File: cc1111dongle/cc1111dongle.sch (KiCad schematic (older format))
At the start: 50 parts, among them J1 GSG-900MHZ-F-ANTENNA, J2 GSG-USB-MICRO-B, P1 EXPANSION, P2 ANTENNA, P3 RESET_N, P4 DD, P5 DC, P6 3V3, P7 GND, P8 GOODFET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

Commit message: finished cc1111dongle schematic
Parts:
- removed J1: GSG-900MHZ-F-ANTENNA, symbol GSG-900MHZ-F-ANTENNA
- removed J2: GSG-USB-MICRO-B, symbol GSG-USB-MICRO-B
- removed P1: EXPANSION, symbol CONN_8X2
- removed P2: ANTENNA, symbol GSG-SMA-CONN
- removed P8: GOODFET, symbol CONN_7X2
- removed P9: PWR, symbol CONN_3X2
- removed R15, R7: 0, symbol R-SHORTED
- removed SW1: SW_PUSH, symbol SW_PUSH
- added C18, C25: 22nF, symbol C
- added C19, C20, C21, C22, C23: 100pF, symbol C
- added C24: 1uF, symbol C
- added FB1: FILTER, symbol FILTER
- added J1: USB-DEVICE, symbol USB-DEVICE
- added L1: 1uH, symbol INDUCTOR
- added P1: EXPANSION, symbol CONN_5X2
- added P2: BNC-CONN, symbol BNC-CONN
- added R1, R15: 4k7, symbol R
- added R3: 1k, symbol R
- added R7: 15, symbol R
- added U3, U8: DMC2400, symbol DMC2400
- added U4: RX_AMP, symbol BGA2717
- added U5, U6: SKY13385, symbol SKY13385
- added U7: TX_AMP, symbol BGA616
- C17: value 10nF -> 1uF; Description CAP CER 10000PF 50V 10% X7R 0603 -> CAP CER 1UF 10V 10% X7R 0603; Manufacturer Murata -> Taiyo Yuden; Note DNP -> (none); Part Number GRM188R71H103KA01D -> LMK107B7105KA-T
- C6: value 10nF -> 220pF; Description CAP CER 10000PF 50V 10% X7R 0603 -> CAP CER 220PF 50V 10% X7R 0402; Part Number GRM188R71H103KA01D -> GRM155R71H221KA01D
- C7: value 10nF -> 220pF; Description CAP CER 10000PF 25V 10% X7R 0402 -> CAP CER 220PF 50V 10% X7R 0402; Part Number GRM155R71E103KA01D -> GRM155R71H221KA01D
- D1, D3, D4, R11, R12: Note DNP -> (none)
- R10, R4, R8, R9: Note (none) -> 1%
- R14: value 10k -> 1k; Description RES 10K OHM 1/10W 5% 0603 SMD -> RES 1K OHM 1/16W 5% 0402 SMD; Part Number RMCF0603JT10K0 -> RMCF0402JT1K00
- R2: value 10k -> 4k7; Description RES 10K OHM 1/10W 5% 0603 SMD -> RES 4.7K OHM 1/16W 5% 0402 SMD; Part Number RMCF0603JT10K0 -> RMCF0402JT4K70
- R6: value 0 -> 4k7; Description (none) -> RES 4.7K OHM 1/16W 5% 0402 SMD; Manufacturer (none) -> Stackpole; Note DNP -> (none); Part Number (none) -> RMCF0402JT4K70
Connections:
- net labels added: AMP_BYPASS_EN, RX_AMP_EN, TX_AMP_EN
- net labels removed: P0_4, P0_5, P1_6, P1_7, P2_0
- wire segments 158 -> 200
- no-connect marks 10 -> 2
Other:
- note added: "RX amp path"
- note added: "RX/TX amp bypass path"
- note added: "TX amp path"
- note removed: "programming header matching GoodFET pinout"
- moved on the sheet: C1, C10, C11, C12, C13, C14, C15, C16, C2, C3, C4, C5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

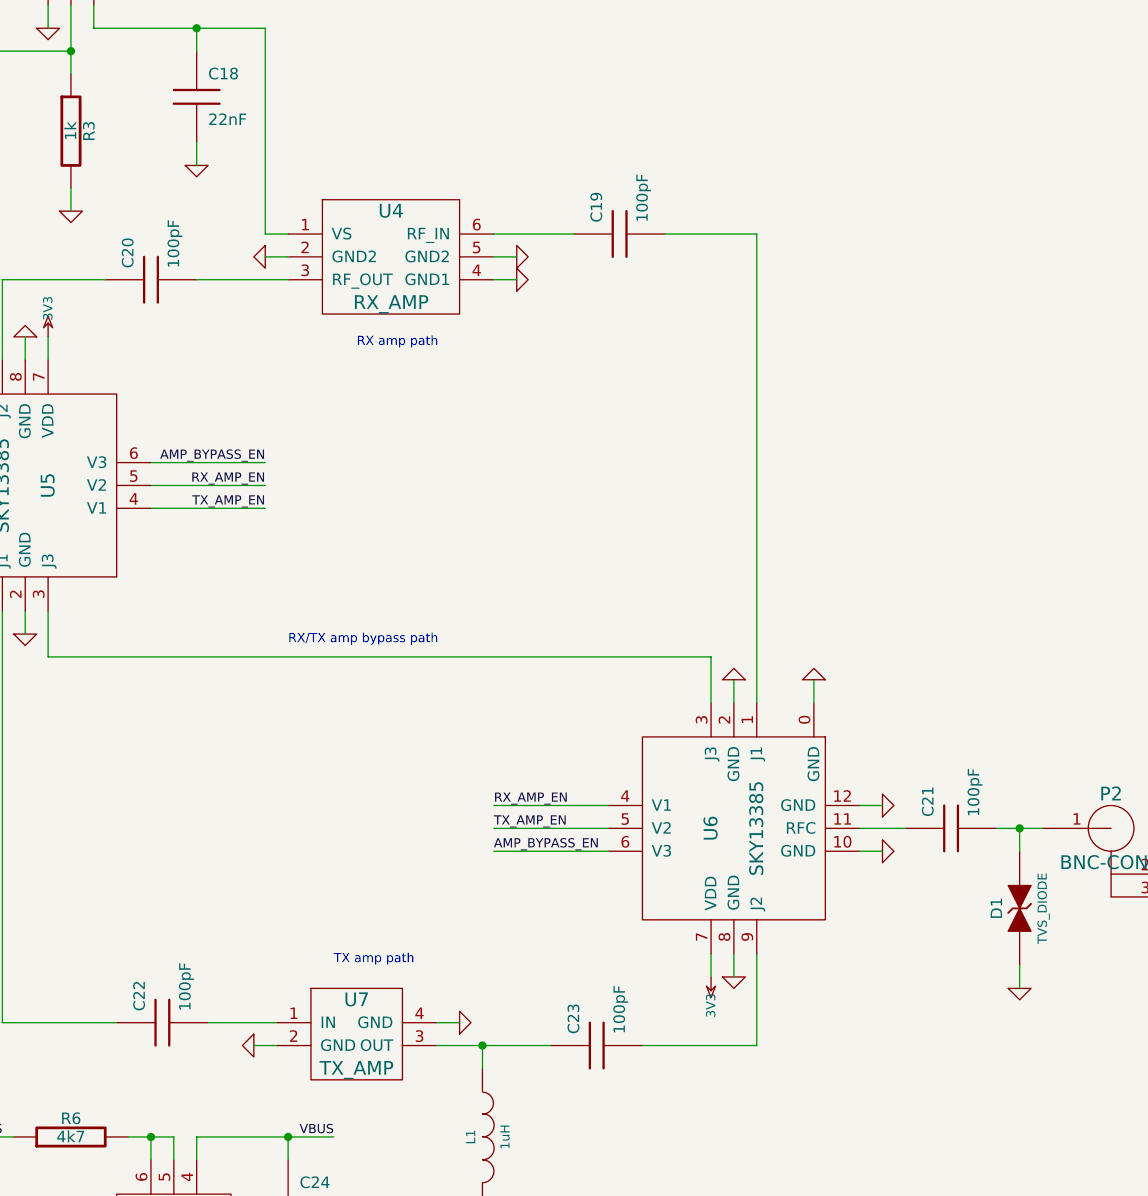
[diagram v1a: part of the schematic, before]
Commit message: replaced some obsolete part numbers
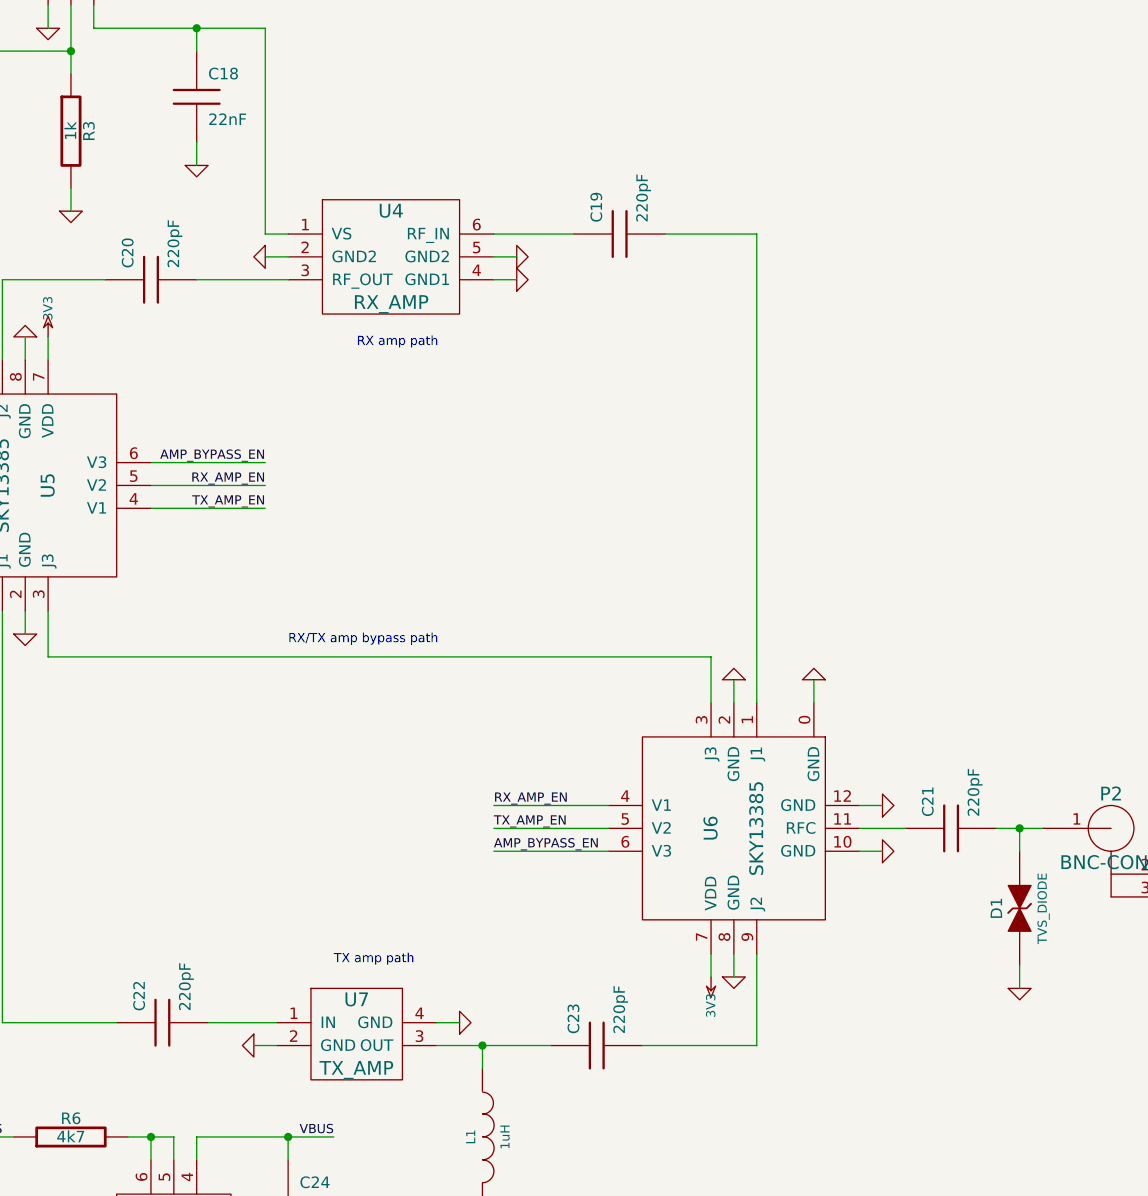
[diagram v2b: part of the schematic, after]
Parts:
- C19, C20, C21, C22, C23: value 100pF -> 220pF; Description CAP CER 100PF 50V 5% NP0 0402 -> CAP CER 220PF 50V 10% X7R 0402; Part Number GRM1555C1H101JZ01D -> GRM155R71H221KA01D
- C9: Manufacturer Murata -> Taiyo Yuden; Part Number GRM1555C1H2R2CZ01D -> UMK105CG2R2CW-F
- U7: Part Number BGA616E6327 -> BGA 616 H6327

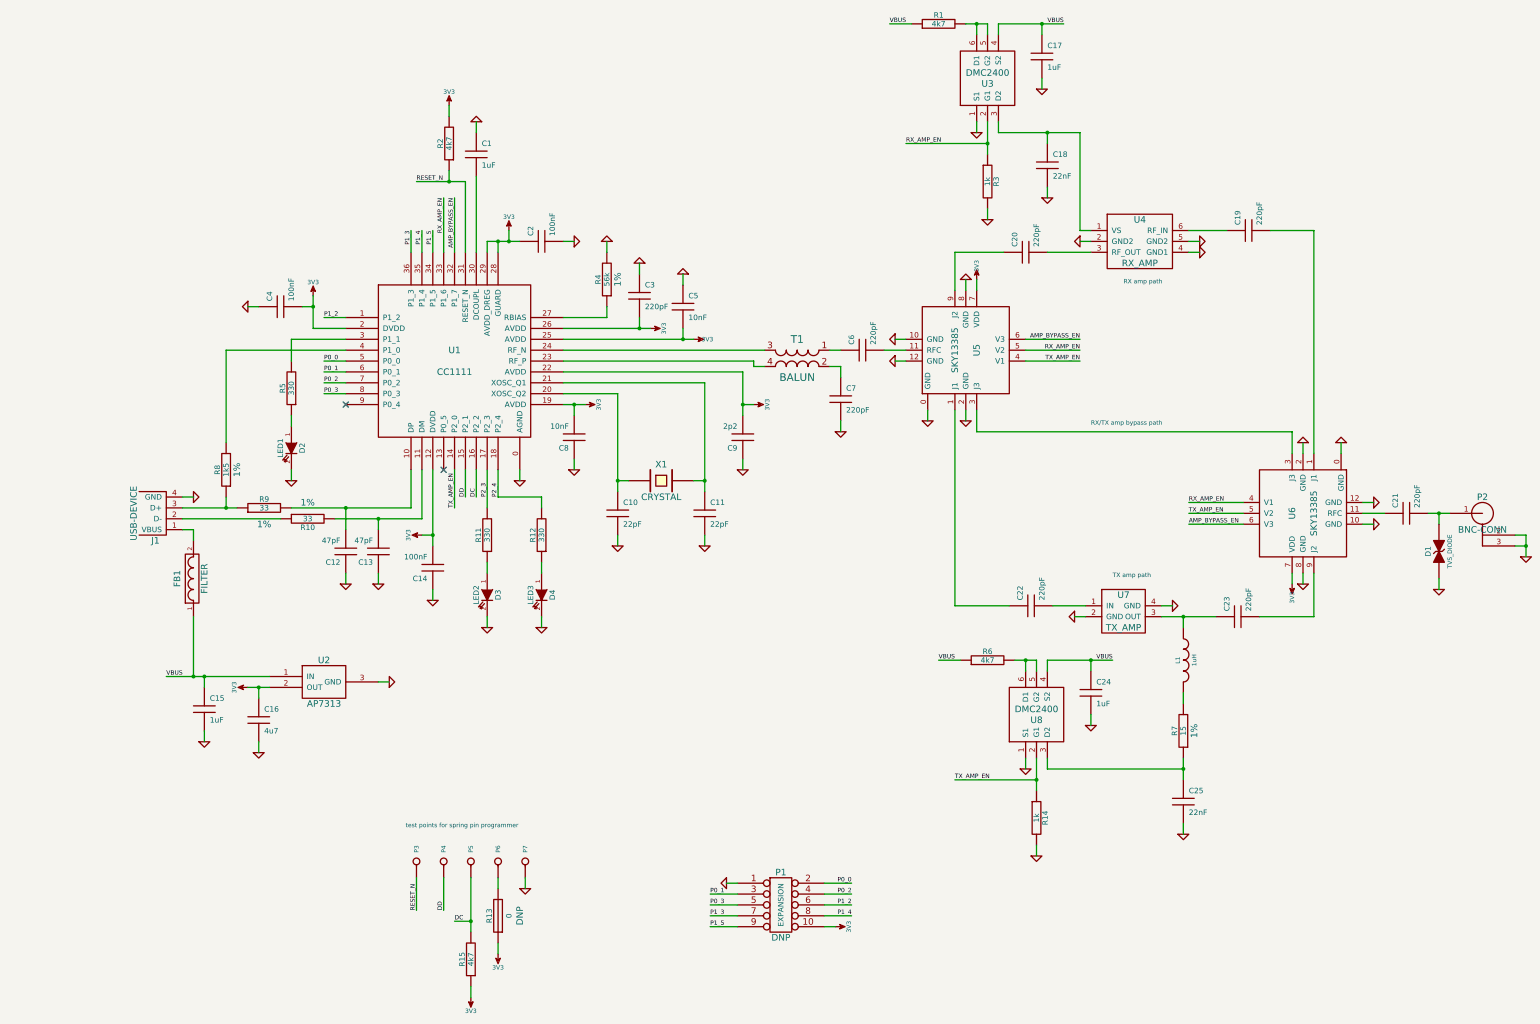
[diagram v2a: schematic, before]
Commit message: extra decoupling based on BGA616 app note
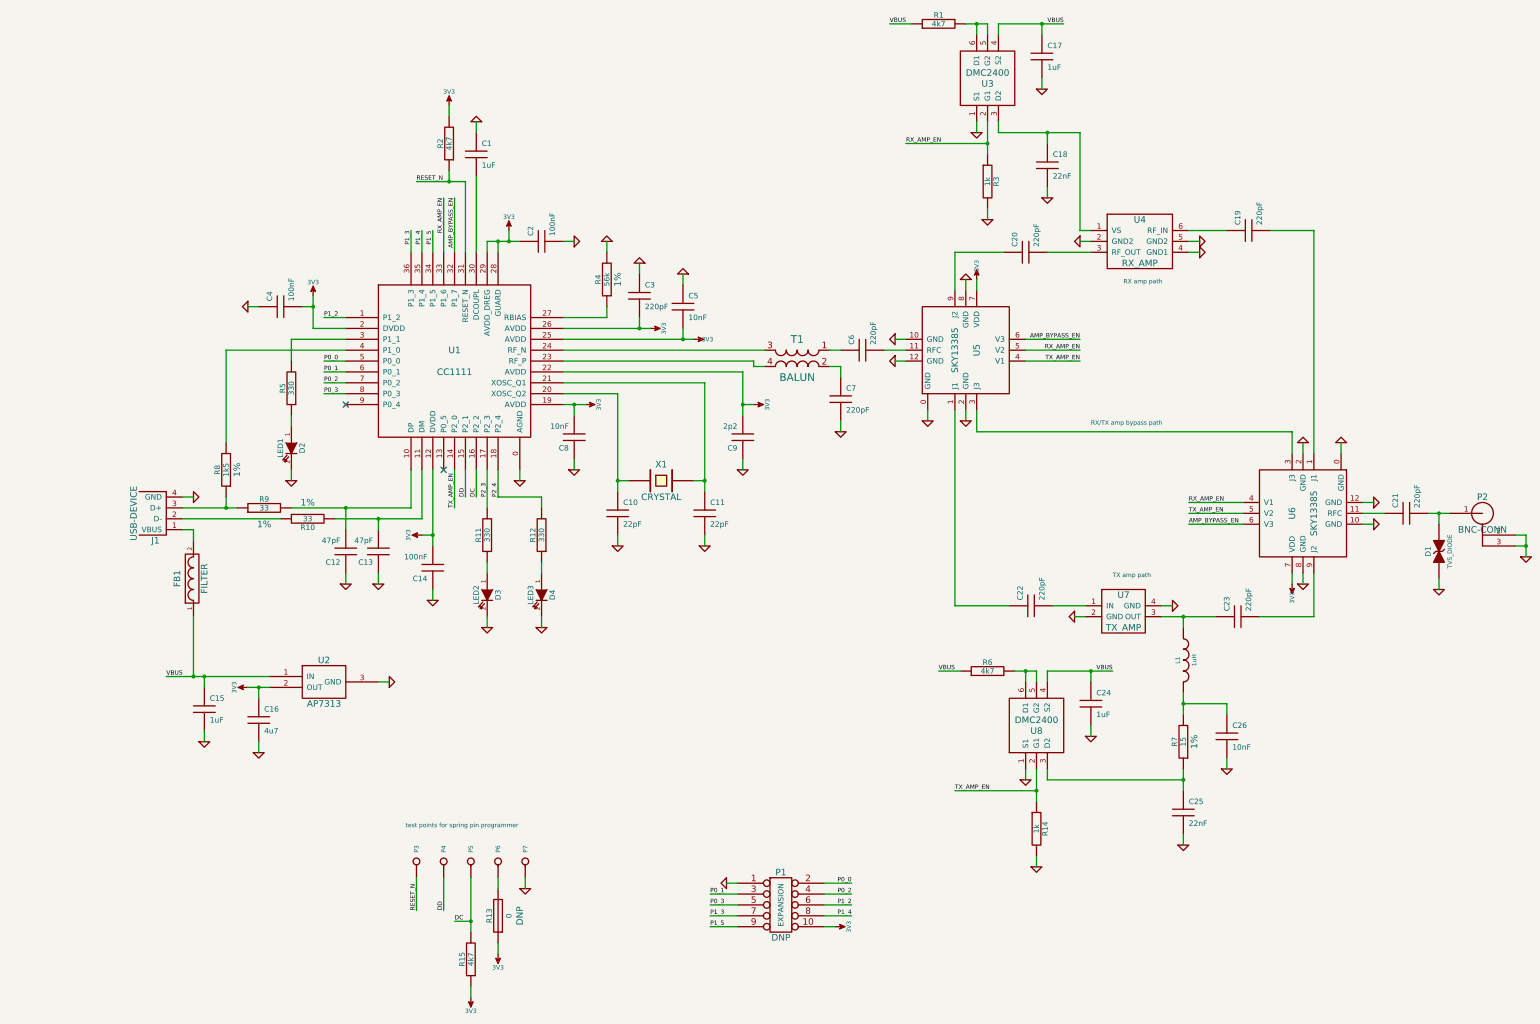
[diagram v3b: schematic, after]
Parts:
- added C26: 10nF, symbol C
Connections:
- net GND: now also C26.2
- net at L1.2, R7.2: now also C26.1
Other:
- moved on the sheet: C24, C25, R14, R6, R7, U8
